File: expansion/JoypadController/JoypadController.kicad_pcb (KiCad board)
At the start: 2 copper layers, 100 x 100 mm, 33 parts, among them J1 D68K_64PIN_BOARD, J2 JTAG, J3 Joystick 1, J4 Joystick 2, U1 74LS125, U2 XC9536PC44, U3 74LS574, U4 74LS574

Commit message: Added JTAG labeling on Joypad board
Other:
- board text added: "GND"
- board text added: "JLCJLCJLCJLC"
- board text added: "TCK"
- board text added: "TDI"
- board text added: "TDO"
- board text added: "TMS"
- board text added: "VCC"

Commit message: Updated PDF schematics for all boards
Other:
- board text added: "© 2021 Stephen Moody"

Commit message: Joypad board, tidied up PCB a little
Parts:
- moved C1 1.74 mm to (190.1, 129.3), turned to 0 degrees

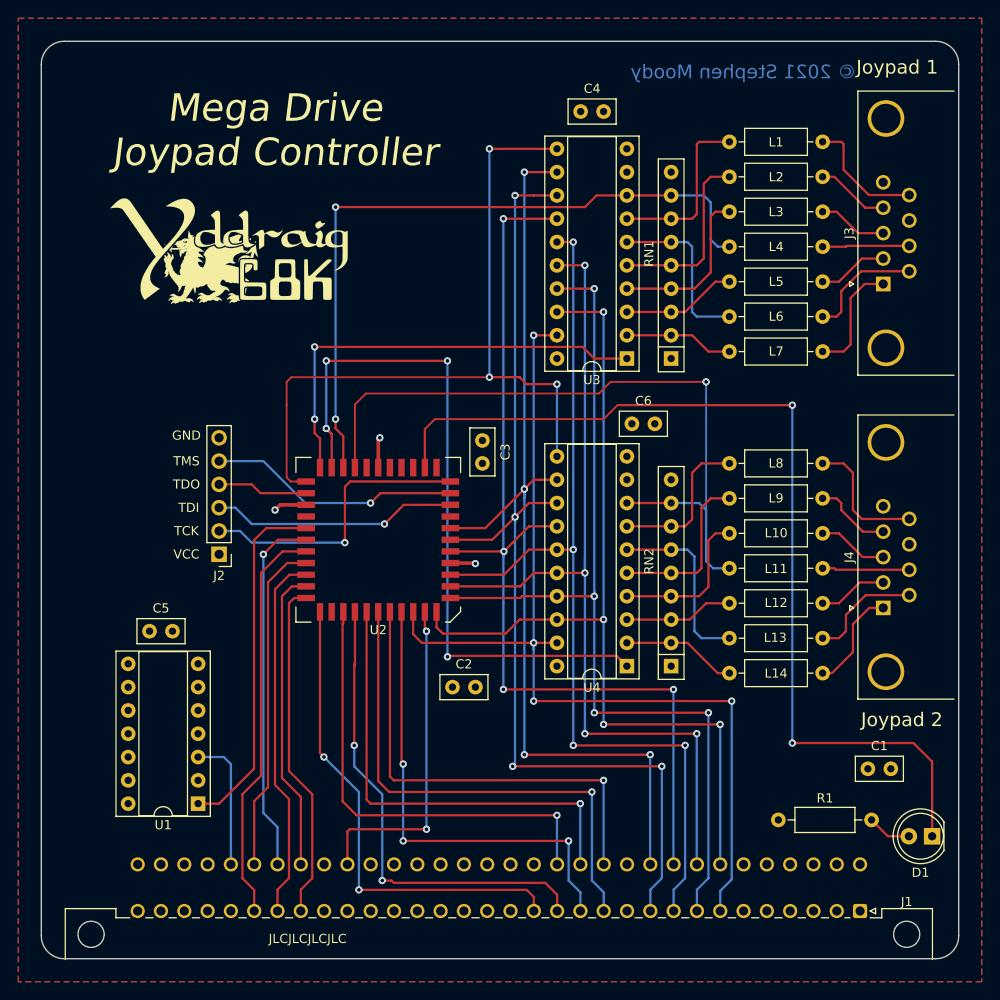
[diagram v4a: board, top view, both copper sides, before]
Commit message: Updated to KiCAD6
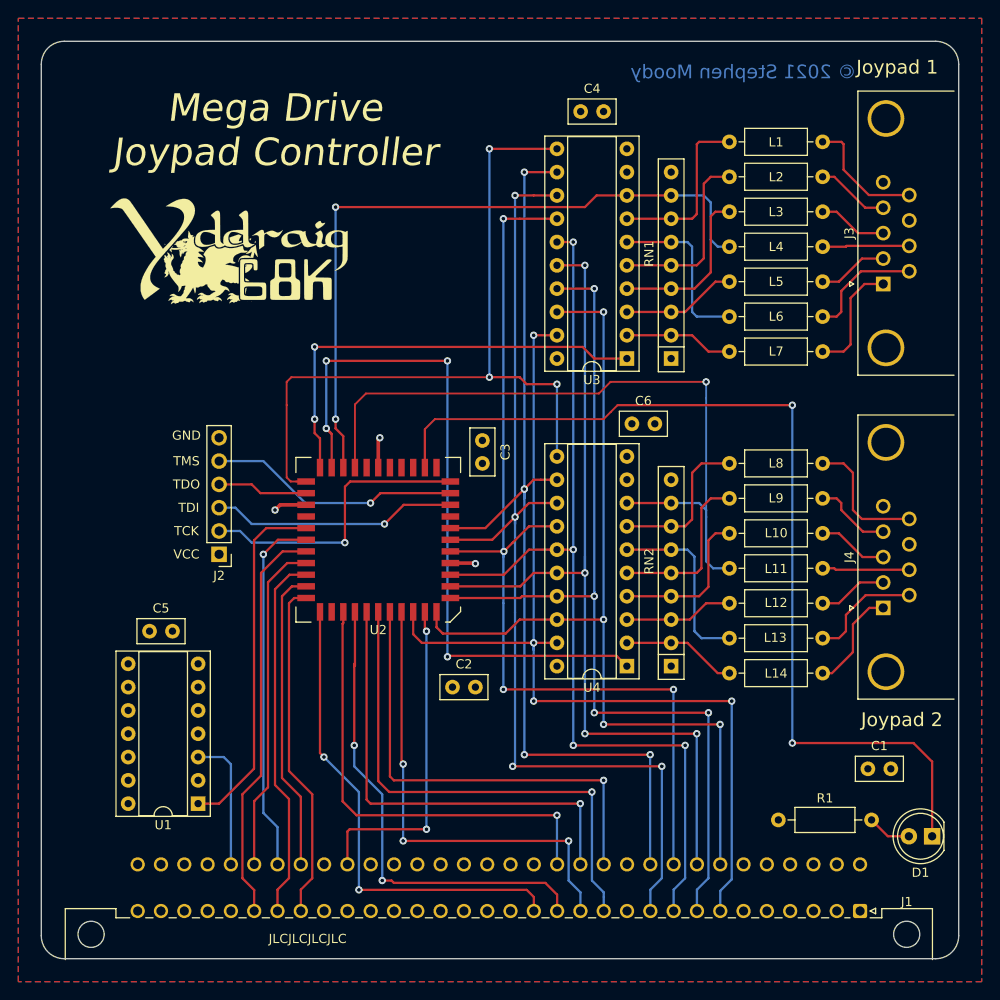
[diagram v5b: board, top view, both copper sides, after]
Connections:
- net /R~W renamed /R~{W}
- net /~CS_DATA renamed /~{CS_DATA}
- net /~CS_REG renamed /~{CS_REG}
- net /~DTACK renamed /~{DTACK}
- net /~JOY1OE renamed /~{JOY1OE}
- net /~JOY2OE renamed /~{JOY2OE}
- net /~LDS renamed /~{LDS}
- net /~RESET renamed /~{RESET}
- net /~UDS renamed /~{UDS}
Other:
- net class Default removed
- net class POWER removed
- net class SIGNAL removed
